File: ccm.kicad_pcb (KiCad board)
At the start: 2 copper layers, 80.1 x 75.2 mm, 61 parts, among them J1 Conn_01x02_Socket, J10 Conn_01x02_Socket, J2 Conn_01x02_Socket, J3 Conn_01x02_Socket, J4 Conn_01x04_Socket, J5 Conn_01x02_Socket, J6 Conn_01x02_Socket, J7 Conn_01x02_Socket, J8 Conn_01x04_Socket, J9 Conn_01x02_Socket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

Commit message: ccm schem complete
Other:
- board text added: "Central Computer Module v2"
- board text removed: "Central Computer Module v1"
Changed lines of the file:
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@@
 		(layer "Edge.Cuts")
 	)
-	(gr_text "Central Computer \nModule v1"
+	(gr_text "Central Computer \nModule v2\n"
 		(at 151.25 133.5 0)
 		(layer "F.SilkS")

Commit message: layout v1
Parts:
- added D1: SS14, Diode_SMD:D_SMA, F.Cu at (99.0, 128.6)
- added D2: SS14, Diode_SMD:D_SMA, F.Cu at (99.2, 82.0)
- added D3: SS14, Diode_SMD:D_SMA, F.Cu at (99.8, 96.5)
- added D4: SS14, Diode_SMD:D_SMA, F.Cu at (100.0, 112.5)
- added J11: Conn_01x02_Socket, Connector_Molex:Molex_Mini-Fit_Jr_5566-02A2_2x01_P4.20mm_Vertical, F.Cu at (92.5, 128.8)
- added J12: Conn_01x02_Socket, Connector_Molex:Molex_Mini-Fit_Jr_5566-02A2_2x01_P4.20mm_Vertical, F.Cu at (92.0, 80.1)
- added J13: Conn_01x02_Socket, Connector_Molex:Molex_Mini-Fit_Jr_5566-02A2_2x01_P4.20mm_Vertical, F.Cu at (166.8, 142.8)
- added J15: Conn_01x02_Socket, Connector_Molex:Molex_Mini-Fit_Jr_5566-02A2_2x01_P4.20mm_Vertical, F.Cu at (92.0, 95.1)
- added J16: Conn_01x02_Socket, Connector_Molex:Molex_Mini-Fit_Jr_5566-02A2_2x01_P4.20mm_Vertical, F.Cu at (92.5, 111.5)
- added J17: Conn_01x02_Socket, Connector_Molex:Molex_Mini-Fit_Jr_5566-02A2_2x01_P4.20mm_Vertical, F.Cu at (152.5, 142.8)
- added J18: Conn_01x02_Socket, Connector_Molex:Molex_Mini-Fit_Jr_5566-02A2_2x01_P4.20mm_Vertical, F.Cu at (138.5, 142.8)
- added J19: Conn_01x02_Socket, Connector_Molex:Molex_Mini-Fit_Jr_5566-02A2_2x01_P4.20mm_Vertical, F.Cu at (201.5, 133.8)
- added J20: Conn_01x02_Socket, Connector_Molex:Molex_Mini-Fit_Jr_5566-02A2_2x01_P4.20mm_Vertical, F.Cu at (180.8, 142.8)
- added J21: Conn_01x02_Socket, Connector_Molex:Molex_Mini-Fit_Jr_5566-02A2_2x01_P4.20mm_Vertical, F.Cu at (202.0, 86.0)
- added J22: Conn_01x02_Socket, Connector_Molex:Molex_Mini-Fit_Jr_5566-02A2_2x01_P4.20mm_Vertical, F.Cu at (201.5, 99.0)
- added J23: Conn_01x02_Socket, Connector_Molex:Molex_Mini-Fit_Jr_5566-02A2_2x01_P4.20mm_Vertical, F.Cu at (201.8, 115.8)
- added J24: Conn_01x02_Socket, Connector_Molex:Molex_Mini-Fit_Jr_5566-02A2_2x01_P4.20mm_Vertical, F.Cu at (92.8, 144.3)
- added Q2: IRLZ34N, Package_TO_SOT_THT:TO-220-3_Vertical, F.Cu at (104.8, 126.5)
- added Q3: IRLZ34N, Package_TO_SOT_THT:TO-220-3_Vertical, F.Cu at (105.1, 78.5)
- added Q4: IRLZ34N, Package_TO_SOT_THT:TO-220-3_Vertical, F.Cu at (105.3, 93.5)
- added Q5: IRLZ34N, Package_TO_SOT_THT:TO-220-3_Vertical, F.Cu at (105.5, 109.5)
- added R33: 220, Resistor_SMD:R_0805_2012Metric, F.Cu at (111.2, 126.0)
- added R34: 10k, Resistor_SMD:R_0805_2012Metric, F.Cu at (110.5, 130.6)
- added R35: 10k, Resistor_SMD:R_0805_2012Metric, F.Cu at (110.0, 84.4)
- added R36: 220, Resistor_SMD:R_0805_2012Metric, F.Cu at (110.0, 79.2)
- added R37: 10k, Resistor_SMD:R_0805_2012Metric, F.Cu at (110.5, 99.7)
- added R38: 220, Resistor_SMD:R_0805_2012Metric, F.Cu at (110.8, 94.0)
- added R39: 10k, Resistor_SMD:R_0805_2012Metric, F.Cu at (110.5, 114.5)
- added R40: 220, Resistor_SMD:R_0805_2012Metric, F.Cu at (110.5, 110.5)
- added R41: 10k, Resistor_SMD:R_0805_2012Metric, F.Cu at (172.2, 114.0)
- added R42: 10k, Resistor_SMD:R_0805_2012Metric, F.Cu at (174.7, 114.0)
- added R43: 10k, Resistor_SMD:R_0805_2012Metric, F.Cu at (172.2, 117.5)
- added R44: 10k, Resistor_SMD:R_0805_2012Metric, F.Cu at (174.7, 117.5)
- moved J1 66.0 mm to (158.0, 68.0), turned to 180 degrees
- moved J7 53.3 mm to (172.2, 68.0), turned to 180 degrees
- moved REF** 24.1 mm to (200.0, 150.0)
- moved J5 22.4 mm to (187.8, 137.8), turned to 90 degrees
- moved REF** 18.1 mm to (114.0, 150.0)
- moved J2 16.3 mm to (123.5, 111.1), turned to -90 degrees
- moved REF** 16.0 mm to (200.0, 66.8)
- moved J10 14.7 mm to (143.4, 68.1)
- moved R22 13.2 mm to (136.2, 127.3), turned to 180 degrees
- moved R5 12.2 mm to (140.8, 127.3)
- moved Q1 11.0 mm to (141.7, 122.0)
- moved R11 11.0 mm to (171.8, 103.0)
- moved R13 11.0 mm to (171.8, 99.9)
- moved R17 11.0 mm to (171.8, 93.7)
- moved R18 11.0 mm to (175.4, 90.7)
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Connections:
- R23 pad 2: unconnected-(R23-Pad2) -> Net-(U1-15_A1_RX3_SPDIF_IN)
- R24 pad 1: unconnected-(R23-Pad2) -> Net-(U1-15_A1_RX3_SPDIF_IN)
- U1 pad 10: unconnected-(U1-8_TX2_IN1-Pad10) -> Fan2_PWM
- U1 pad 18: unconnected-(U1-26_A12_MOSI1-Pad18) -> Net-(U1-26_A12_MOSI1)
- U1 pad 19: unconnected-(U1-27_A13_SCK1-Pad19) -> Net-(U1-27_A13_SCK1)
- U1 pad 20: unconnected-(U1-28_RX7-Pad20) -> Net-(U1-28_RX7)
- U1 pad 21: unconnected-(U1-29_TX7-Pad21) -> Net-(U1-29_TX7)
- U1 pad 25: unconnected-(U1-33_MCLK2-Pad25) -> gpio1
- U1 pad 26: unconnected-(U1-34_RX8-Pad26) -> gpio2
- U1 pad 27: unconnected-(U1-35_TX8-Pad27) -> gpio3
- U1 pad 28: unconnected-(U1-36_CS-Pad28) -> gpio4
- U1 pad 31: unconnected-(U1-39_MISO1_OUT1A-Pad31) -> Net-(U1-39_MISO1_OUT1A)
- U1 pad 32: unconnected-(U1-40_A16-Pad32) -> thermistor3+
- U1 pad 33: unconnected-(U1-41_A17-Pad33) -> thermistor2+
- U1 pad 36: unconnected-(U1-14_A0_TX3_SPDIF_OUT-Pad36) -> thermistor1+
- U1 pad 37: unconnected-(R23-Pad2) -> Net-(U1-15_A1_RX3_SPDIF_IN)
- U1 pad 9: unconnected-(U1-7_RX2_OUT1A-Pad9) -> Fan1_PWM
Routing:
- net acc_ped_2: track 33.3 -> 0.00 mm
- net acc_ped_1: track 31.6 -> 0.00 mm
- net ready_to_drive_button: track 72.2 -> 44.0 mm
- net lin_pot_2: track 25.9 -> 0.00 mm
- net lin_pot_1: track 24.7 -> 0.00 mm
- net brake_light: track 24.5 -> 0.00 mm
- net rtm_sound: track 24.2 -> 0.09 mm
- net brake_2: track 23.5 -> 0.00 mm
- net brake_1: track 22.9 -> 0.00 mm
- net GLV-: track 95.3 -> 77.7 mm, vias 22 -> 21
- net lin_pot_4: track 17.6 -> 0.00 mm
- net lin_pot_3: track 16.9 -> 0.00 mm
- net PWM_in_2: track 20.5 -> 6.89 mm
- net unconnected-(R23-Pad2): track 11.9 -> 0.00 mm
- net Net-(U1-15_A1_RX3_SPDIF_IN): track 0.00 -> 11.9 mm
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- added copper zone on B.Cu, net thermistor1-
- added copper zone on F.Cu, net thermistor1-
- removed copper zone on B.Cu, net GLV-
- removed copper zone on F.Cu, net GLV-
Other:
- board size 80.1 x 75.2 mm -> 96 x 93.2 mm
- board text added: "CCM V2"
- board text removed: "Central Computer Module v2"

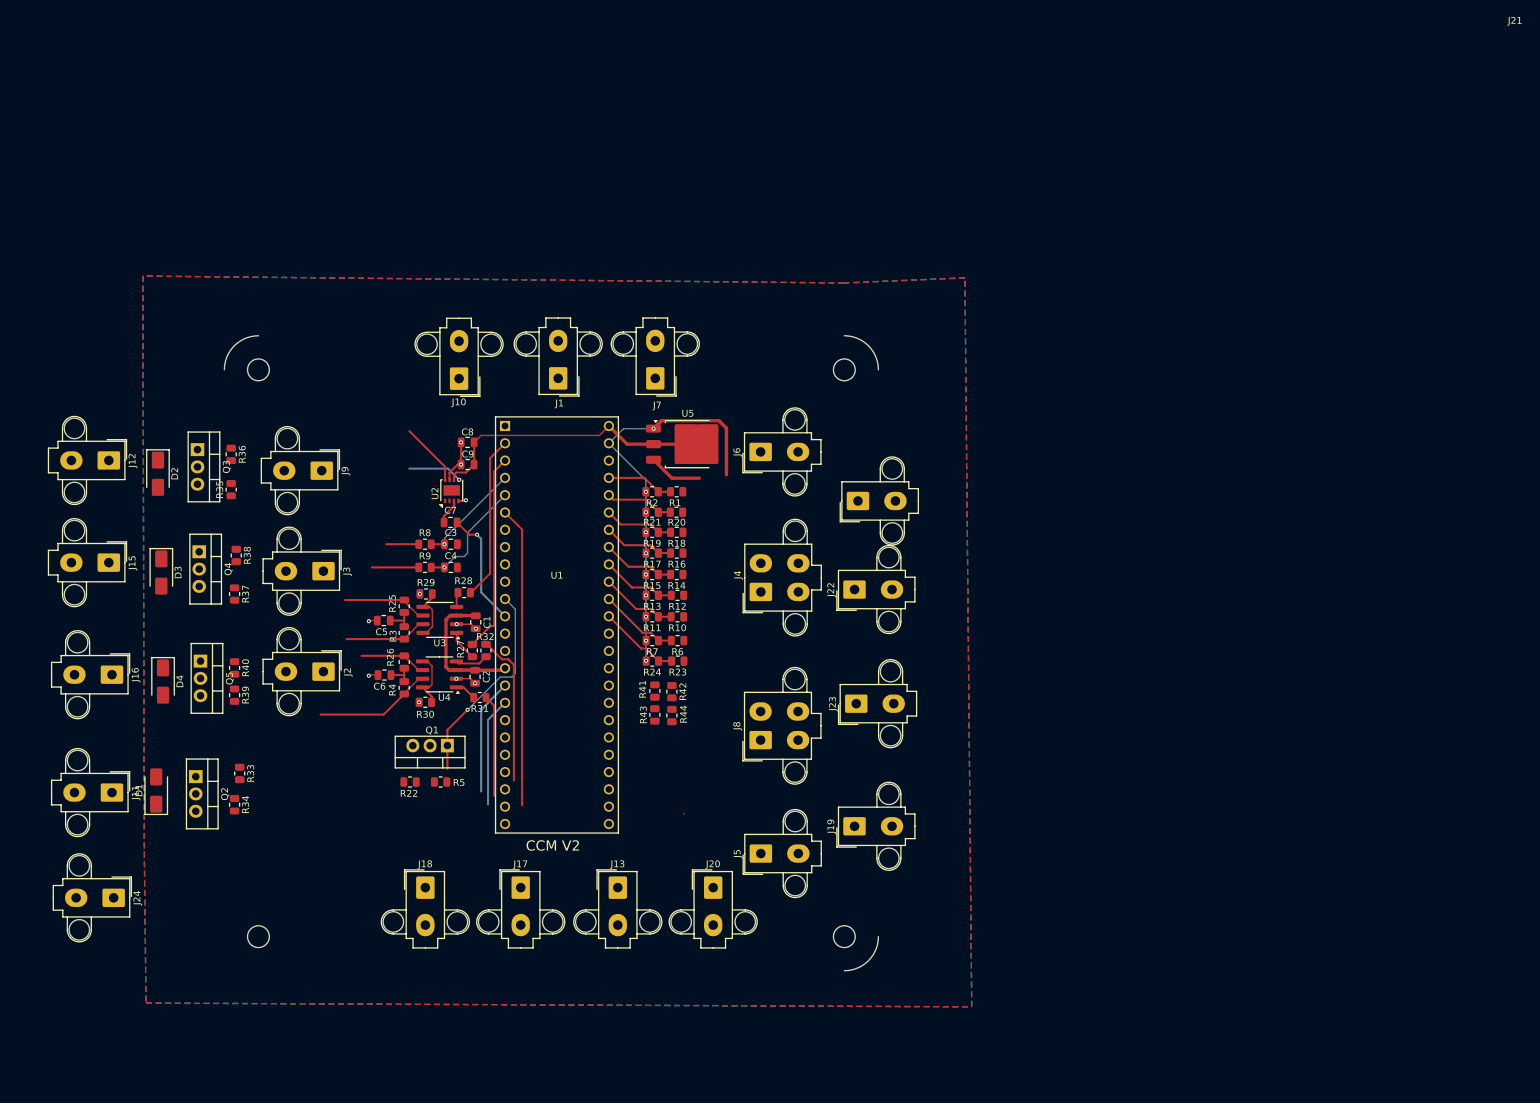
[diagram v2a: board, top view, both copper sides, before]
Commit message: leftside routing complete
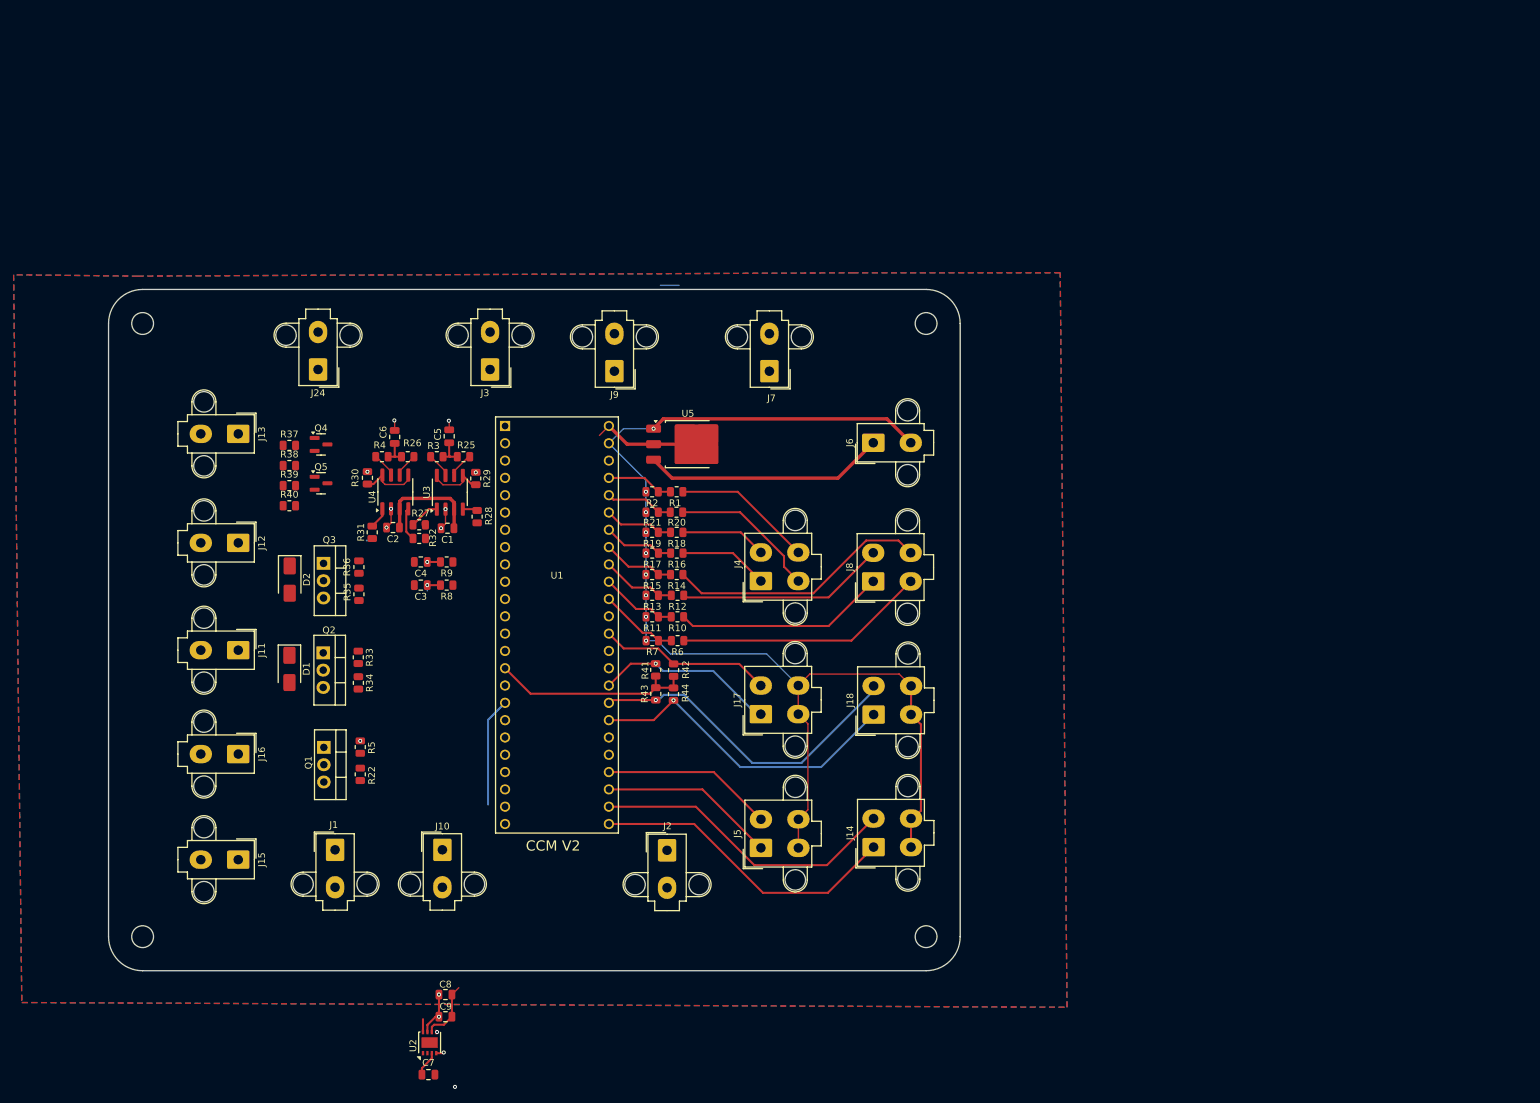
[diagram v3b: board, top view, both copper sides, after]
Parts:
- removed D3, D4: SS14, Diode_SMD:D_SMA
- removed J19, J20, J21, J22, J23: Conn_01x02_Socket, Connector_Molex:Molex_Mini-Fit_Jr_5566-02A2_2x01_P4.20mm_Vertical
- removed R23: 1k, Resistor_SMD:R_0805_2012Metric
- removed R24: 3k, Resistor_SMD:R_0805_2012Metric
- added J14: Conn_01x04_Socket, Connector_Molex:Molex_Mini-Fit_Jr_5566-04A2_2x02_P4.20mm_Vertical, F.Cu at (204.3, 136.9)
- D1, D2: value SS14 -> SS34
- J17, J18, J5: value Conn_01x02_Socket -> Conn_01x04_Socket; footprint Connector_Molex:Molex_Mini-Fit_Jr_5566-02A2_2x01_P4.20mm_Vertical -> Connector_Molex:Molex_Mini-Fit_Jr_5566-04A2_2x02_P4.20mm_Vertical
- Q4, Q5: value IRLZ34N -> MMBT3904; footprint Package_TO_SOT_THT:TO-220-3_Vertical -> Package_TO_SOT_SMD:SOT-23
- R38: value 220 -> 10k
- R39: value 10k -> 1k
- R40: value 220 -> 1k
- moved REF** 128.6 mm to (212.0, 150.0)
- moved REF** 103.0 mm to (97.0, 150.0)
- moved REF** 91.6 mm to (97.0, 60.0)
- moved J13 86.8 mm to (111.0, 76.2), turned to -90 degrees
- moved J24 83.2 mm to (122.8, 66.8), turned to 180 degrees
- moved U2 81.1 mm to (139.1, 165.6)
- moved C7 81.1 mm to (138.9, 170.2)
- moved C8 81.1 mm to (141.4, 158.5)
- moved C9 81.1 mm to (141.4, 161.8)
- moved J1 76.6 mm to (125.2, 137.2), turned to 0 degrees
- moved J18 70.5 mm to (204.3, 117.4), turned to 90 degrees
- moved J10 69.2 mm to (141.0, 137.2), turned to 0 degrees
- moved J2 56.8 mm to (174.0, 137.3), turned to 0 degrees
- moved J15 47.6 mm to (111.0, 138.7)
- moved J9 45.4 mm to (166.2, 67.0), turned to 180 degrees
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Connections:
- J13 pad 1: gpio3 -> Fan1+
- J15 pad 2: Fan1- -> GLV-
- J16 pad 2: Fan2- -> GLV-
- J17 pad 1: gpio1 -> thermistor2+
- J17 pad 2: GLV- -> thermistor1+
- J18 pad 1: gpio2 -> thermistor4+
- J18 pad 2: GLV- -> thermistor3+
- J5 pad 1: rtm_sound -> gpio2
- J5 pad 2: unconnected-(J5-Pin_2-Pad2) -> gpio1
- J8 pad 1: brake_2 -> brake_1
- J8 pad 2: brake_1 -> acc_ped_2
- J8 pad 3: acc_ped_2 -> brake_2
- Q4 pad 1: Net-(Q4-G) -> Net-(Q4-B)
- Q4 pad 2: Fan1- -> GLV-
- Q4 pad 3: GLV- -> Fan1_PWM
- Q5 pad 2: Fan2- -> GLV-
- Q5 pad 3: GLV- -> Fan2_PWM
- R37 pad 1: Net-(U1-28_RX7) -> +5V
- R37 pad 2: GLV- -> Fan1_PWM
- R38 pad 1: Net-(Q4-G) -> +5V
- R38 pad 2: Net-(U1-28_RX7) -> Fan2_PWM
- R39 pad 1: Net-(U1-29_TX7) -> Net-(Q4-B)
- R40 pad 2: Net-(U1-29_TX7) -> Net-(U1-8_TX2_IN1)
- R44 pad 1: Net-(U1-39_MISO1_OUT1A) -> thermistor4+
- U1 pad 10: Fan2_PWM -> Net-(U1-8_TX2_IN1)
- U1 pad 20: Net-(U1-28_RX7) -> unconnected-(U1-28_RX7-Pad20)
- U1 pad 21: Net-(U1-29_TX7) -> unconnected-(U1-29_TX7-Pad21)
- U1 pad 25: gpio1 -> gpio4
- U1 pad 26: gpio2 -> gpio3
- U1 pad 27: gpio3 -> gpio2
- U1 pad 28: gpio4 -> gpio1
- U1 pad 31: Net-(U1-39_MISO1_OUT1A) -> thermistor4+
- U1 pad 37: Net-(U1-15_A1_RX3_SPDIF_IN) -> unconnected-(U1-15_A1_RX3_SPDIF_IN-Pad37)
- U1 pad 9: Fan1_PWM -> GLV-
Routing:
- net GLV-: track 77.7 -> 188.4 mm, vias 21 -> 20
- net thermistor3+: track 0.00 -> 48.6 mm, vias 0 -> 1
- net thermistor4+: track 0.00 -> 47.3 mm, vias 0 -> 1
- net gpio4: track 0.00 -> 45.8 mm
- net gpio3: track 0.00 -> 45.2 mm
- net ready_to_drive_button: track 44.0 -> 0.00 mm
- net acc_ped_1: track 0.00 -> 38.5 mm
- net brake_2: track 0.00 -> 36.9 mm
- net brake_1: track 0.00 -> 31.1 mm
- net Net-(Q1-G): track 30.7 -> 0.00 mm
- net acc_ped_2: track 0.00 -> 30.7 mm
- net CAN_TX_1: track 29.7 -> 0.48 mm
- net Vin: track 7.82 -> 35.5 mm
- net thermistor2+: track 0.00 -> 26.7 mm, vias 0 -> 1
- net +3.3V: track 20.6 -> 46.5 mm
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- added copper zone on B.Cu, net GLV-
- added copper zone on F.Cu, net GLV-
- removed copper zone on B.Cu, net thermistor1-
- removed copper zone on F.Cu, net thermistor1-
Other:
- board size 96 x 93.2 mm -> 125 x 100 mm

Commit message: routing v2.1 complete
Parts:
- added C10: 10nF, Capacitor_SMD:C_0805_2012Metric, F.Cu at (142.9, 123.1)
- added R23: 1k, Resistor_SMD:R_0805_2012Metric, F.Cu at (142.8, 119.8)
- R1, R10, R12, R14, R16, R18, R20, R6: value 1k -> 50k
- R11, R13, R15, R17, R19, R2, R21, R7: value 1k -> 97k
- moved C3 50.1 mm to (175.6, 65.5)
- moved R8 50.1 mm to (179.4, 65.5)
- moved C4 46.1 mm to (175.6, 68.5)
- moved R9 46.1 mm to (179.4, 68.5)
- moved C7 44.0 mm to (142.9, 126.4)
- moved U2 35.8 mm to (143.0, 129.9), turned to -90 degrees
- moved C8 31.0 mm to (138.8, 127.7)
- moved C9 31.0 mm to (138.8, 130.9)
- moved R38 11.4 mm to (124.6, 71.1)
- moved R40 11.3 mm to (125.4, 77.9)
- moved Q5 9.17 mm to (125.5, 74.6), turned to 90 degrees
- moved R37 7.22 mm to (121.0, 71.1), turned to 180 degrees
- moved R39 6.13 mm to (120.1, 77.9)
- moved D2 5.32 mm to (117.5, 92.4)
- moved Q3 5.32 mm to (122.5, 90.0)
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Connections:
- C1 pad 2: GLV- -> Pump1-
- C2 pad 2: GLV- -> Pump1-
- C3 pad 2: GLV- -> Pump1-
- C4 pad 2: GLV- -> Pump1-
- C5 pad 2: GLV- -> Pump1-
- C6 pad 2: GLV- -> Pump1-
- C7 pad 2: speaker_pwm -> Net-(C10-Pad2)
- C8 pad 2: GLV- -> Pump1-
- C9 pad 2: GLV- -> Pump1-
- D2 pad 2: Pump2- -> Pump1-
- J12 pad 2: Pump2- -> Pump1-
- J13 pad 2: GLV- -> Pump1-
- J14 pad 3: GLV- -> Pump1-
- J14 pad 4: GLV- -> Pump1-
- J15 pad 2: GLV- -> Pump1-
- J16 pad 2: GLV- -> Pump1-
- J17 pad 3: GLV- -> Pump1-
- J17 pad 4: GLV- -> Pump1-
- J18 pad 3: GLV- -> Pump1-
- J18 pad 4: GLV- -> Pump1-
- J5 pad 3: GLV- -> Pump1-
- J5 pad 4: GLV- -> Pump1-
- J6 pad 2: GLV- -> Pump1-
- Q1 pad 3: GLV- -> Pump1-
- Q2 pad 3: GLV- -> Pump1-
- Q3 pad 2: Pump2- -> Pump1-
- Q3 pad 3: GLV- -> Pump1-
- Q4 pad 2: GLV- -> Pump1-
- Q5 pad 2: GLV- -> Pump1-
- R11 pad 2: GLV- -> Pump1-
- R13 pad 2: GLV- -> Pump1-
- R15 pad 2: GLV- -> Pump1-
- R17 pad 2: GLV- -> Pump1-
- R19 pad 2: GLV- -> Pump1-
- R2 pad 2: GLV- -> Pump1-
- R21 pad 2: GLV- -> Pump1-
- R22 pad 1: GLV- -> Pump1-
- R29 pad 1: GLV- -> Pump1-
- R30 pad 1: GLV- -> Pump1-
- R33 pad 2: Net-(U1-26_A12_MOSI1) -> Net-(U1-27_A13_SCK1)
- R34 pad 1: Net-(U1-26_A12_MOSI1) -> Net-(U1-27_A13_SCK1)
- R34 pad 2: GLV- -> Pump1-
- R35 pad 1: Net-(U1-27_A13_SCK1) -> Net-(U1-26_A12_MOSI1)
- R35 pad 2: GLV- -> Pump1-
- R36 pad 2: Net-(U1-27_A13_SCK1) -> Net-(U1-26_A12_MOSI1)
- R39 pad 2: GLV- -> Net-(U1-8_TX2_IN1)
- R40 pad 2: Net-(U1-8_TX2_IN1) -> Net-(U1-7_RX2_OUT1A)
- R5 pad 1: GLV- -> Pump1-
- R7 pad 2: GLV- -> Pump1-
- R8 pad 1: PWM_in_1 -> PWM_in_2
- R9 pad 1: PWM_in_2 -> PWM_in_1
- U1 pad 1: GLV- -> Pump1-
- U1 pad 47: GLV- -> Pump1-
- U1 pad 9: GLV- -> Net-(U1-7_RX2_OUT1A)
- U2 pad 4: GLV- -> Pump1-
- U2 pad 7: GLV- -> Pump1-
- U3 pad 2: GLV- -> Pump1-
- U4 pad 2: GLV- -> Pump1-
- U5 pad 1: GLV- -> Pump1-
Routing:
- net Pump1-: track 0.00 -> 324.2 mm, vias 0 -> 23
- net GLV-: track 188.4 -> 0.00 mm, vias 20 -> 0
- net Fan1+: track 0.00 -> 134.7 mm
- net +5V: track 23.9 -> 155.2 mm
- net ready_to_drive_button: track 0.00 -> 68.9 mm, vias 0 -> 1
- net CAN_TX_2: track 0.00 -> 61.8 mm
- net CAN_RX_2: track 0.13 -> 52.5 mm
- net Net-(U1-8_TX2_IN1): track 0.00 -> 39.1 mm
- net Net-(U1-26_A12_MOSI1): track 0.00 -> 38.7 mm
- net Net-(Q1-G): track 0.00 -> 37.2 mm, vias 1 -> 2
- net i2c_SCL: track 0.06 -> 36.4 mm
- net Net-(U1-7_RX2_OUT1A): track 0.00 -> 34.7 mm
- net Net-(U1-3_LRCLK2): track 1.94 -> 35.2 mm
- net CANH_1: track 3.82 -> 36.7 mm
- net Net-(U1-2_OUT2): track 2.78 -> 35.4 mm
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- added copper zone on B.Cu, net Pump1-
- added copper zone on F.Cu, net Pump1-
- removed copper zone on B.Cu, net GLV-
- removed copper zone on F.Cu, net GLV-
